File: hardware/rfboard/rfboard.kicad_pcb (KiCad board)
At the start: 2 copper layers, 21 x 44 mm, 20 parts, among them J1 10118194-0001LF, P2 CONN_01X03, P3 CONN_01X04, U1 SAMD21E18, U2 RFM69CW-915MHZ, U3 MIC5504-3.3YM5-T5, U4 74LVC1G125

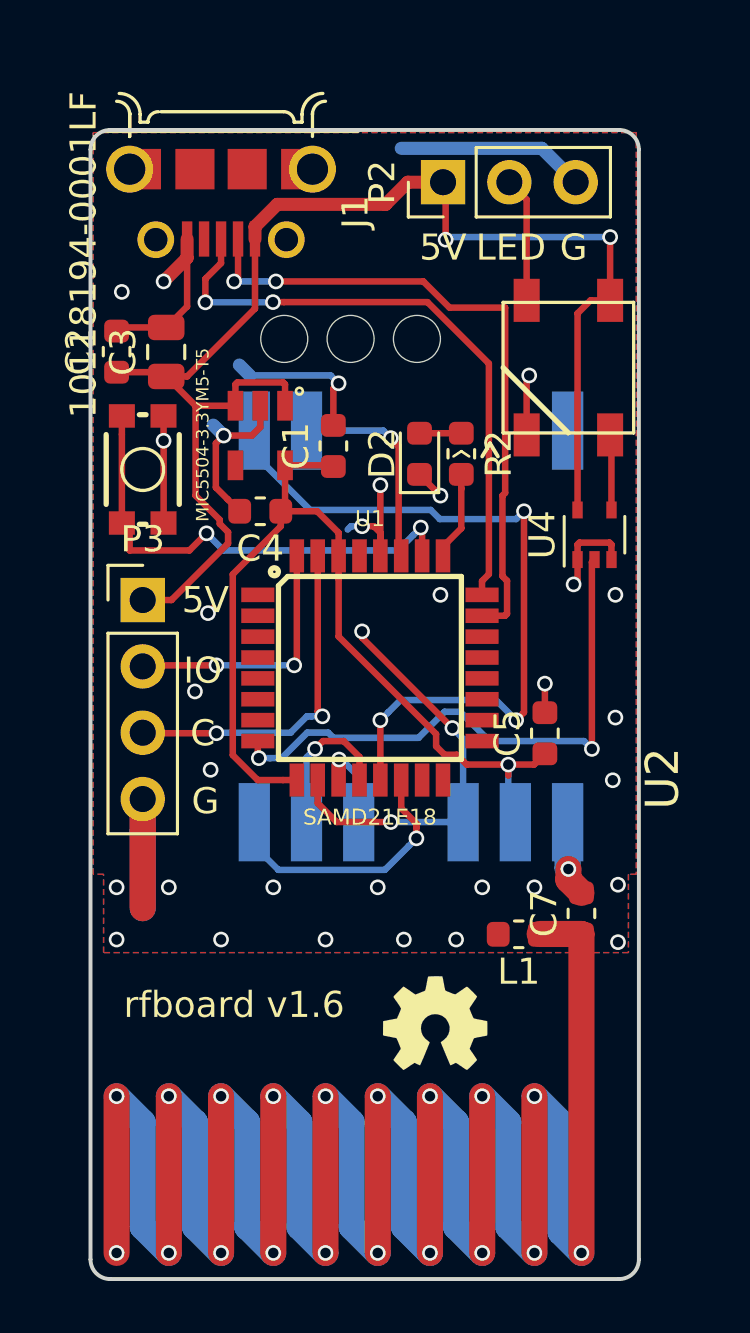
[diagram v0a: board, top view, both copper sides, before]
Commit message: Update rfboard to KiCAD 6
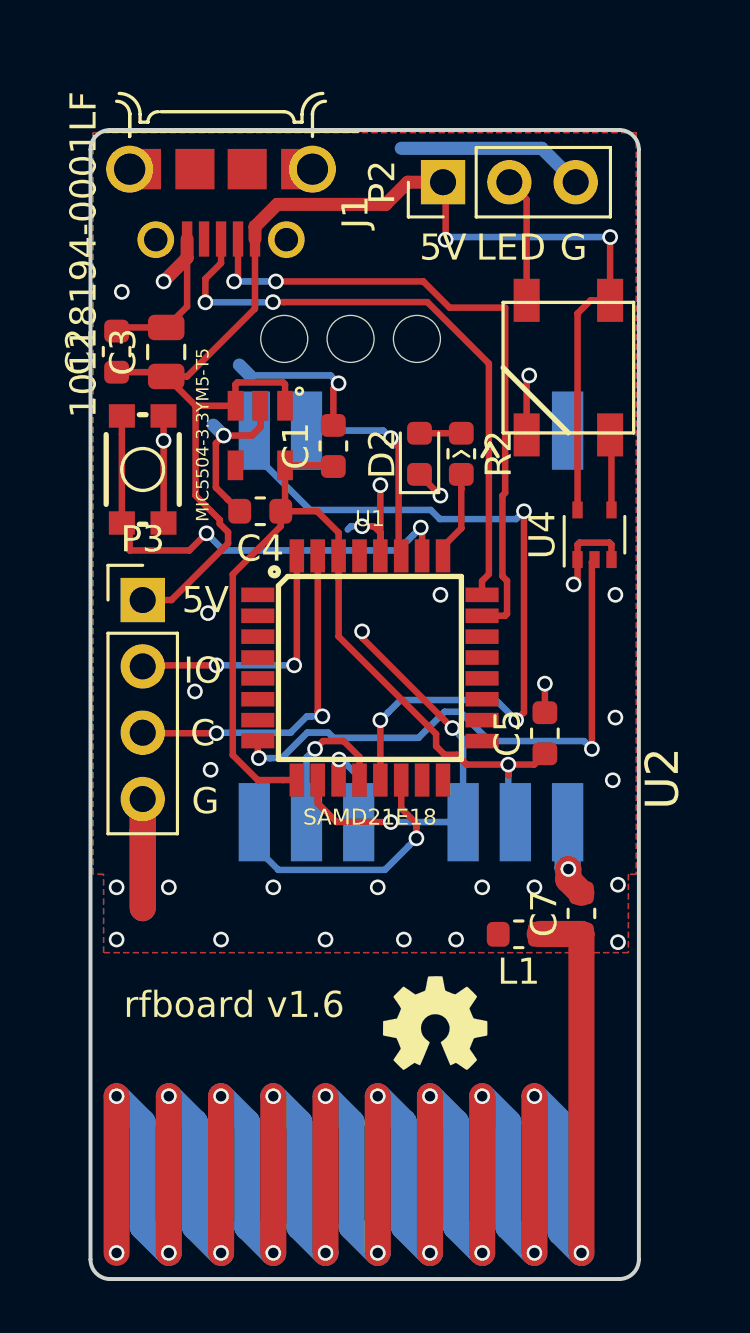
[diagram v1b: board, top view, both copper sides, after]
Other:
- net class Default removed
